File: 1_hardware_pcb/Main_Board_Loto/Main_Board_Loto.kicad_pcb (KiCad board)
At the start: 2 copper layers, 138 x 119 mm, 77 parts, among them J1 Conn_01x05_Pin, J1 FTDI, J2 Conn_01x05_Pin, J2 V+-, J3 Conn_01x05_Pin, J4 Conn_01x05_Pin, J5 MOTOR_PINM1A, J6 MOTOR_PINM1B, J7 MOTOR_PINM1A, J8 MOTOR_PINM1B, Q1 2N7002, SW1 SW_SPST, SW2 START, SW3 START, U1 AMS1117-3.3, U1 QRE1113GR, U2 LM7805_TO220, U2 QRE1113GR, U3 QRE1113GR, U3 TA6586, U4 ESP32-WROOM-32, U4 QRE1113GR, U5 QRE1113GR, U5 TA6586, U6 QRE1113GR, U7 QRE1113GR, U8 QRE1113GR

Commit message: SCH terminado
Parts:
- removed BOOT1, EN1: SW_Push, Button_Switch_THT:SW_PUSH_6mm_H5mm
- removed the C1 at (134.2, 80.1)
- removed the C1 at (147.7, 47.8)
- removed the C2 at (144.1, 46.8)
- removed the C2 at (98.4, 105.0)
- removed D3: LED, EESTN5-v2:Led_0805
- removed the H1 at (107.5, 46.5)
- removed the H1 at (112.1, 124.5)
- removed the H2 at (175.9, 124.5)
- removed the H2 at (180.5, 46.5)
- removed the J1 at (202.3, 110.1)
- removed the J1 at (162.3, 44.8)
- removed the J2 at (115.1, 44.8)
- removed the J2 at (97.0, 95.5)
- removed J6, J8: MOTOR_PINM1B, Connector:Banana_Jack_1Pin
- removed J7: MOTOR_PINM1A, Connector:Banana_Jack_1Pin
- removed the R1 at (194.2, 106.6)
- removed the R1 at (172.3, 35.1)
- removed the R2 at (183.2, 98.4)
- removed the R2 at (163.0, 35.1)
- removed the R3 at (113.2, 113.5)
- removed the R3 at (153.7, 35.1)
- removed the R4 at (116.9, 113.5)
- removed the R4 at (144.5, 35.1)
- removed the R5 at (178.9, 40.0)
- removed the R5 at (116.3, 107.9)
- removed the R6 at (120.5, 113.5)
- removed the R6 at (169.6, 40.0)
- removed the R7 at (160.3, 40.0)
- removed the R7 at (124.8, 107.9)
- removed the R8 at (171.6, 109.7)
- removed the R8 at (151.1, 40.0)
- removed the U1 at (140.5, 83.5)
- removed the U1 at (176.4, 36.9)
- removed the U2 at (101.8, 103.5)
- removed the U2 at (167.1, 36.9)
- removed the U3 at (138.6, 133.3)
- removed the U3 at (157.8, 36.9)
- removed the U4 at (140.2, 110.5)
- removed the U4 at (148.5, 36.9)
- removed the U5 at (156.9, 133.3)
- removed the U5 at (139.2, 36.9)
- added C1: 1uF, Capacitor_SMD:C_0805_2012Metric_Pad1.18x1.45mm_HandSolder, B.Cu at (400.8, 82.1)
- added C2: 1uF, Capacitor_SMD:C_0805_2012Metric_Pad1.18x1.45mm_HandSolder, B.Cu at (397.8, 87.3)
- added G***: LOGO, LOGO, F.Cu at (432.3, 115.2)
- added H1: Mounting_Hole, EESTN5:hole_3mm, F.Cu at (399.4, 111.4)
- added H2: Mounting_Hole, EESTN5:hole_3mm, F.Cu at (399.4, 134.8)
- added H7: HOLE, EESTN5:Separador_M3_5mm, F.Cu at (437.2, 168.2)
- added H8: HOLE, EESTN5:Separador_M3_5mm, F.Cu at (437.2, 175.4)
- added J1: V+-, EESTN5:BORNERA2_AZUL, F.Cu at (380.4, 101.8)
- added J2: MOTOR_PINM1A, Connector:Banana_Jack_1Pin, F.Cu at (425.4, 152.6)
- added R1: 220, EESTN5:R_1206, B.Cu at (406.9, 98.3)
- added R17: 100, EESTN5:R_1206, B.Cu at (391.9, 46.7)
- added R18: 10k, EESTN5:R_1206, B.Cu at (425.7, 45.9)
- added R19: 10k, EESTN5:R_1206, B.Cu at (413.9, 47.6)
- added R2: 4K7, EESTN5:R_1206, B.Cu at (462.4, 102.4)
- added R20: 10k, EESTN5:R_1206, B.Cu at (402.0, 48.7)
- added R21: 10k, EESTN5:R_1206, B.Cu at (391.9, 50.2)
- added R3: 220, EESTN5:R_1206, B.Cu at (407.0, 105.5)
- added R4: 10K, EESTN5:R_1206, B.Cu at (428.6, 96.0)
- added R5: 4K7, EESTN5:R_1206, B.Cu at (471.7, 102.8)
- added R6: 100, EESTN5:R_1206, B.Cu at (470.4, 53.4)
- added R7: 100, EESTN5:R_1206, B.Cu at (460.7, 49.8)
- added R8: 100, EESTN5:R_1206, B.Cu at (449.6, 44.4)
- added U1: AMS1117-3.3, Package_TO_SOT_SMD:SOT-223-3_TabPin2, B.Cu at (407.1, 78.5)
- added U10: QRE1113GR, OptoDevice:OnSemi_CASE100CY, B.Cu at (425.7, 39.1)
- added U11: QRE1113GR, OptoDevice:OnSemi_CASE100CY, B.Cu at (413.8, 40.5)
- added U12: QRE1113GR, OptoDevice:OnSemi_CASE100CY, B.Cu at (401.9, 41.9)
- added U13: QRE1113GR, OptoDevice:OnSemi_CASE100CY, B.Cu at (391.8, 43.5)
- added U2: LM7805_TO220, Package_TO_SOT_THT:TO-220-3_Vertical, F.Cu at (395.9, 91.1)
- added U3: TA6586, Package_DIP:DIP-8_W7.62mm, F.Cu at (423.5, 136.1)
- added U4: ESP32_DevKit_V1_CH9102X, EESTN5:ESP32_DevKit_V1_CH9102X, F.Cu at (433.3, 100.4)
- added U5: TA6586, Package_DIP:DIP-8_W7.62mm, F.Cu at (454.2, 136.2)
- added U9: QRE1113GR, OptoDevice:OnSemi_CASE100CY, B.Cu at (437.1, 39.2)
- BZ1: footprint EESTN5-v2:Buzzer_12mm -> EESTN5:Buzzer_12mm
- C3: value 1n -> 1uF; footprint EESTN5-v2:C_0805 -> Capacitor_SMD:C_0805_2012Metric_Pad1.18x1.45mm_HandSolder
- C5: value 1uF -> 0.1uF; footprint Capacitor_SMD:C_0805_2012Metric_Pad1.18x1.45mm_HandSolder -> EESTN5:C_0805
- C6: value 1n -> 100uF; footprint EESTN5-v2:C_0805 -> Capacitor_THT:CP_Radial_D5.0mm_P2.50mm; moved to F.Cu
- C7: value 0.1uF -> 100nf; footprint EESTN5-v2:C_0805 -> Capacitor_SMD:C_0805_2012Metric_Pad1.18x1.45mm_HandSolder
- C8: value 100uF -> 100uf; footprint Capacitor_THT:CP_Radial_D5.0mm_P2.50mm -> Capacitor_THT:C_Radial_D5.0mm_H11.0mm_P2.00mm
- C9: footprint EESTN5-v2:C_0805 -> EESTN5:C_0805
- D1, D2: footprint EESTN5-v2:Led_0805 -> EESTN5:led_5mm_clear
- H3, H4, H5, H6: footprint EESTN5-v2:hole_3mm -> EESTN5:hole_3mm
- J3: value Conn_01x05_Pin -> MOTOR_PINM1B; footprint Connector_PinHeader_2.54mm:PinHeader_1x05_P2.54mm_Horizontal -> Connector:Banana_Jack_1Pin
- J4: value Conn_01x05_Pin -> MOTOR_PINM1A; footprint Connector_PinHeader_2.54mm:PinHeader_1x05_P2.54mm_Horizontal -> Connector:Banana_Jack_1Pin
- J5: value MOTOR_PINM1A -> MOTOR_PINM1B
- R10, R11, R12: value 100 -> 10k; footprint EESTN5-v2:R_0805 -> EESTN5:R_1206
- R13, R9: footprint EESTN5-v2:R_0805 -> EESTN5:R_1206
- R14, R15, R16: value 10k -> 100; footprint EESTN5-v2:R_0805 -> EESTN5:R_1206
- SW1: value SW_SPST -> START; footprint EESTN5-v2:SW_SPDT_TH_Vertical -> Button_Switch_THT:SW_PUSH_6mm_H5mm
- SW2: value START -> SW_SPST; footprint Button_Switch_THT:SW_PUSH_6mm_H5mm -> EESTN5:SW_SPDT_TH_Vertical
- moved SW1 372.8 mm to (462.4, 93.9), turned to 0 degrees
- moved SW3 353.1 mm to (471.9, 93.9), turned to 0 degrees
- moved H4 351.6 mm to (463.4, 134.8), turned to 0 degrees
- moved J4 347.2 mm to (456.4, 152.8), turned to 0 degrees
- moved R10 344.8 mm to (470.4, 48.9), turned to 0 degrees
- moved R11 344.3 mm to (460.7, 45.0), turned to 0 degrees
- moved R12 342.6 mm to (449.6, 47.8), turned to 0 degrees
- moved U6 340.6 mm to (470.4, 45.7)
- moved U7 340.1 mm to (460.7, 42.1)
- moved U8 338.3 mm to (449.6, 40.9)
- moved C8 337.2 mm to (455.7, 75.2), turned to 180 degrees
- moved H6 334.6 mm to (429.9, 175.4), turned to 0 degrees
- moved C7 317.5 mm to (455.7, 82.2), turned to 180 degrees
- moved C9 316.2 mm to (444.4, 135.0)
- moved C5 310.6 mm to (413.7, 134.9), turned to -90 degrees
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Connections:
- C3 pad 1: GND -> +3V3
- C3 pad 2: /BOOT -> GND
- C4 pad 1: +3V3 -> +5V
- C5 pad 1: +5V -> VCC
- C6 pad 1: GND -> VCC
- C6 pad 2: /EN -> GND
- C7 pad 1: VCC -> +3V3
- C8 pad 1: VCC -> +3V3
- J3 pad 1: /OUT_4 -> /OUTM1B
- J4 pad 1: /OUT_8 -> /OUTM2A
- J5 pad 1: /OUTM1A -> /OUTM2B
- R10 pad 1: +3V3 -> /OUT_1
- R10 pad 2: Net-(U6-A) -> +3V3
- R11 pad 1: +3V3 -> /OUT_2
- R11 pad 2: Net-(U7-A) -> +3V3
- R12 pad 1: +3V3 -> /OUT_3
- R12 pad 2: Net-(U8-A) -> +3V3
- R13 pad 1: /OUT_5 -> /OUT_4
- R14 pad 1: /OUT_6 -> +3V3
- R14 pad 2: +3V3 -> Net-(U10-A)
- R15 pad 1: /OUT_7 -> +3V3
- R15 pad 2: +3V3 -> Net-(U11-A)
- R16 pad 1: /OUT_8 -> +3V3
- R16 pad 2: +3V3 -> Net-(U12-A)
- SW1 pad 1: VCC -> GND
- SW1 pad 2: Net-(SW1-B) -> /PUSH_1
- SW2 pad 1: GND -> VCC
- SW2 pad 2: /PUSH_1 -> Net-(SW2-B)
- U6 pad 3: /OUT_6 -> /OUT_1
- U7 pad 3: /OUT_7 -> /OUT_2
- U8 pad 3: /OUT_8 -> /OUT_3
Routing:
- net +3V3: track 369.3 -> 158.7 mm, vias 1 -> 0
- net /BOOT: track 102.2 -> 0.00 mm, vias 3 -> 0
- net +5V: track 137.7 -> 42.9 mm, vias 2 -> 0
- net /Tx: track 71.6 -> 0.00 mm, vias 1 -> 0
- net /Rx: track 67.4 -> 0.00 mm, vias 1 -> 0
- net /EN: track 59.4 -> 0.00 mm, vias 1 -> 0
- net /BUZZER: track 51.3 -> 109.5 mm, vias 1 -> 0
- net /PUSH_1: track 44.3 -> 85.1 mm, vias 1 -> 0
- net /OUT_8: track 39.2 -> 77.7 mm
- net /PUSH_2: track 39.8 -> 71.9 mm, vias 1 -> 0
- net VCC: track 122.1 -> 94.6 mm
- net /OUT_7: track 37.2 -> 64.1 mm
- net /OUT_1: track 50.5 -> 77.1 mm
- net /OUT_2: track 47.2 -> 67.1 mm
- net Net-(SW2-B): track 0.00 -> 20.0 mm
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- removed copper zone on B.Cu, net /OUTM1A
- removed copper zone on F.Cu, net /OUTM1A
- removed copper zone on B.Cu, net /OUTM1B
- removed copper zone on F.Cu, net /OUTM1B
- removed copper zone on B.Cu, net /OUTM2A
- removed copper zone on F.Cu, net /OUTM2A
- removed copper zone on B.Cu, net /OUTM2B
- removed copper zone on F.Cu, net /OUTM2B
- removed copper zone on B.Cu, net GND
- removed copper zone on F.Cu, net GND
- removed copper zone on B.Cu, net VCC
- removed copper zone on F.Cu, net VCC
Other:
- board outline removed

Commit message: Definida la ubicacion de los componentes y enrutadas las vias de los mismos
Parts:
- removed the C2 at (397.8, 87.3)
- removed H5, H6: Mounting_Hole, EESTN5:hole_3mm
- removed H7, H8: HOLE, EESTN5:Separador_M3_5mm
- added C6: 100nf, Capacitor_SMD:C_0805_2012Metric_Pad1.18x1.45mm_HandSolder, B.Cu at (142.0, 47.2)
- moved C2 395.7 mm to (60.2, 86.7), turned to 90 degrees
- moved C5 391.8 mm to (65.7, 44.5), turned to 90 degrees
- moved R4 345.8 mm to (82.8, 96.5), turned to 0 degrees
- moved R7 337.2 mm to (123.8, 36.9), turned to 90 degrees
- moved R6 337.0 mm to (133.8, 38.2), turned to 90 degrees
- moved R8 336.0 mm to (113.8, 35.0), turned to 90 degrees
- moved Q1 335.6 mm to (87.9, 95.6), turned to 0 degrees
- moved R9 333.5 mm to (103.8, 33.8), turned to 90 degrees
- moved U7 332.4 mm to (128.2, 39.2)
- moved U6 332.2 mm to (138.2, 40.5)
- moved R14 332.1 mm to (93.8, 33.8), turned to 90 degrees
- moved U8 331.3 mm to (118.2, 37.3)
- moved SW1 331.3 mm to (131.1, 87.6)
- moved SW3 331.3 mm to (140.6, 87.6)
- moved R15 330.2 mm to (83.8, 35.3), turned to 90 degrees
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- renumbered C8 to C2, C7 to C5, C5 to C7, C6 to C8
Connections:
- C2 pad 1: +3V3 -> VCC
- J1 pad 2: VCC -> /SWITCH
- SW2 pad 1: VCC -> /SWITCH
- SW2 pad 2: Net-(SW2-B) -> VCC
- U2 pad 1: Net-(SW2-B) -> VCC
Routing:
- net GND: track 348.9 -> 122.4 mm, vias 0 -> 9
- net +3V3: track 158.7 -> 287.3 mm
- net /BUZZER: track 109.5 -> 45.5 mm
- net /LED_1: track 39.1 -> 86.9 mm
- net /LED_2: track 41.6 -> 76.7 mm
- net VCC: track 94.6 -> 121.3 mm
- net Net-(SW2-B): track 20.0 -> 0.00 mm
- net /SWITCH: track 0.00 -> 12.0 mm
- net /OUT_8: track 77.7 -> 68.2 mm
- net Net-(D1-A): track 11.6 -> 3.28 mm
- net Net-(D2-A): track 13.0 -> 5.65 mm
- net /OUT_7: track 64.1 -> 57.6 mm
- net /PUSH_2: track 71.9 -> 65.6 mm
- net Net-(BZ1-+): track 4.23 -> 10.4 mm
- net /PUSH_1: track 85.1 -> 79.8 mm
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- added copper zone on B.Cu, net GND
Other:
- board outline added: 138.7 x 158.6 mm

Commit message: Cntorno de PCB diseñad en FreeCAD y PCB terminad en Kicad
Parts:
- C2: footprint Capacitor_THT:C_Radial_D5.0mm_H11.0mm_P2.00mm -> Capacitor_THT:C_Radial_D10.0mm_H12.5mm_P5.00mm
- moved G*** 185.7 mm to (-82.5, 99.2)
- moved C2 118.1 mm to (177.9, 77.0), turned to 180 degrees
- moved C4 113.6 mm to (186.5, 63.9), turned to 180 degrees
- moved U2 113.1 mm to (182.5, 66.7), turned to 0 degrees
- moved U1 109.6 mm to (194.4, 66.2)
- moved C3 108.8 mm to (199.0, 61.5), turned to 180 degrees
- moved C1 108.5 mm to (186.5, 69.2)
- moved R2 106.0 mm to (239.9, 82.6), turned to 90 degrees
- moved R5 105.8 mm to (249.3, 82.6), turned to 90 degrees
- moved J3 105.8 mm to (190.4, 141.3)
- moved SW1 105.7 mm to (236.5, 79.0)
- moved SW3 105.7 mm to (246.0, 79.0)
- moved R4 105.2 mm to (187.6, 87.3)
- moved Q1 105.2 mm to (192.7, 86.3)
- moved BZ1 104.9 mm to (197.3, 82.5), turned to 90 degrees
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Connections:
- net /OUT_1 renamed /QRE_1
- net /OUT_2 renamed /QRE_2
- net /OUT_3 renamed /QRE_3
- net /OUT_4 renamed /QRE_4
- net /OUT_5 renamed /QRE_5
- net /OUT_6 renamed /QRE_6
- net /OUT_7 renamed /QRE_7
- net /OUT_8 renamed /QRE_8
- U4 pad 21: /PUSH_2 -> /PUSH_1
- U4 pad 22: /PUSH_1 -> /PUSH_2
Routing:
- net VCC: track 121.3 -> 77.2 mm
- net /PUSH_1: track 79.8 -> 48.9 mm
- net GND: track 122.4 -> 100.2 mm
- net /OUTM1A: track 19.0 -> 0.00 mm
- net /OUTM1B: track 17.1 -> 0.00 mm
- net /OUTM2A: track 15.2 -> 0.00 mm
- net /OUTM2B: track 14.6 -> 0.00 mm
- net +5V: track 40.2 -> 26.9 mm
- net /SWITCH: track 12.0 -> 0.00 mm
- net /PUSH_2: track 65.6 -> 56.6 mm
- net Net-(BZ1-+): track 10.4 -> 3.63 mm
- net /QRE_7: track 57.6 -> 54.4 mm
- net /M1A: track 34.3 -> 37.4 mm
- net /M1B: track 33.9 -> 37.0 mm
- net /QRE_6: track 51.2 -> 48.1 mm
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- added copper zone on B.Cu, net +3V3
- added copper zone on B.Cu, net /OUTM1A
- added copper zone on B.Cu, net /OUTM1B
- added copper zone on B.Cu, net /OUTM2A
- added copper zone on B.Cu, net /OUTM2B
- added copper zone on B.Cu, net /SWITCH
- added copper zone on B.Cu, net VCC
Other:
- board size 138.7 x 158.6 mm -> 138.1 x 157.3 mm

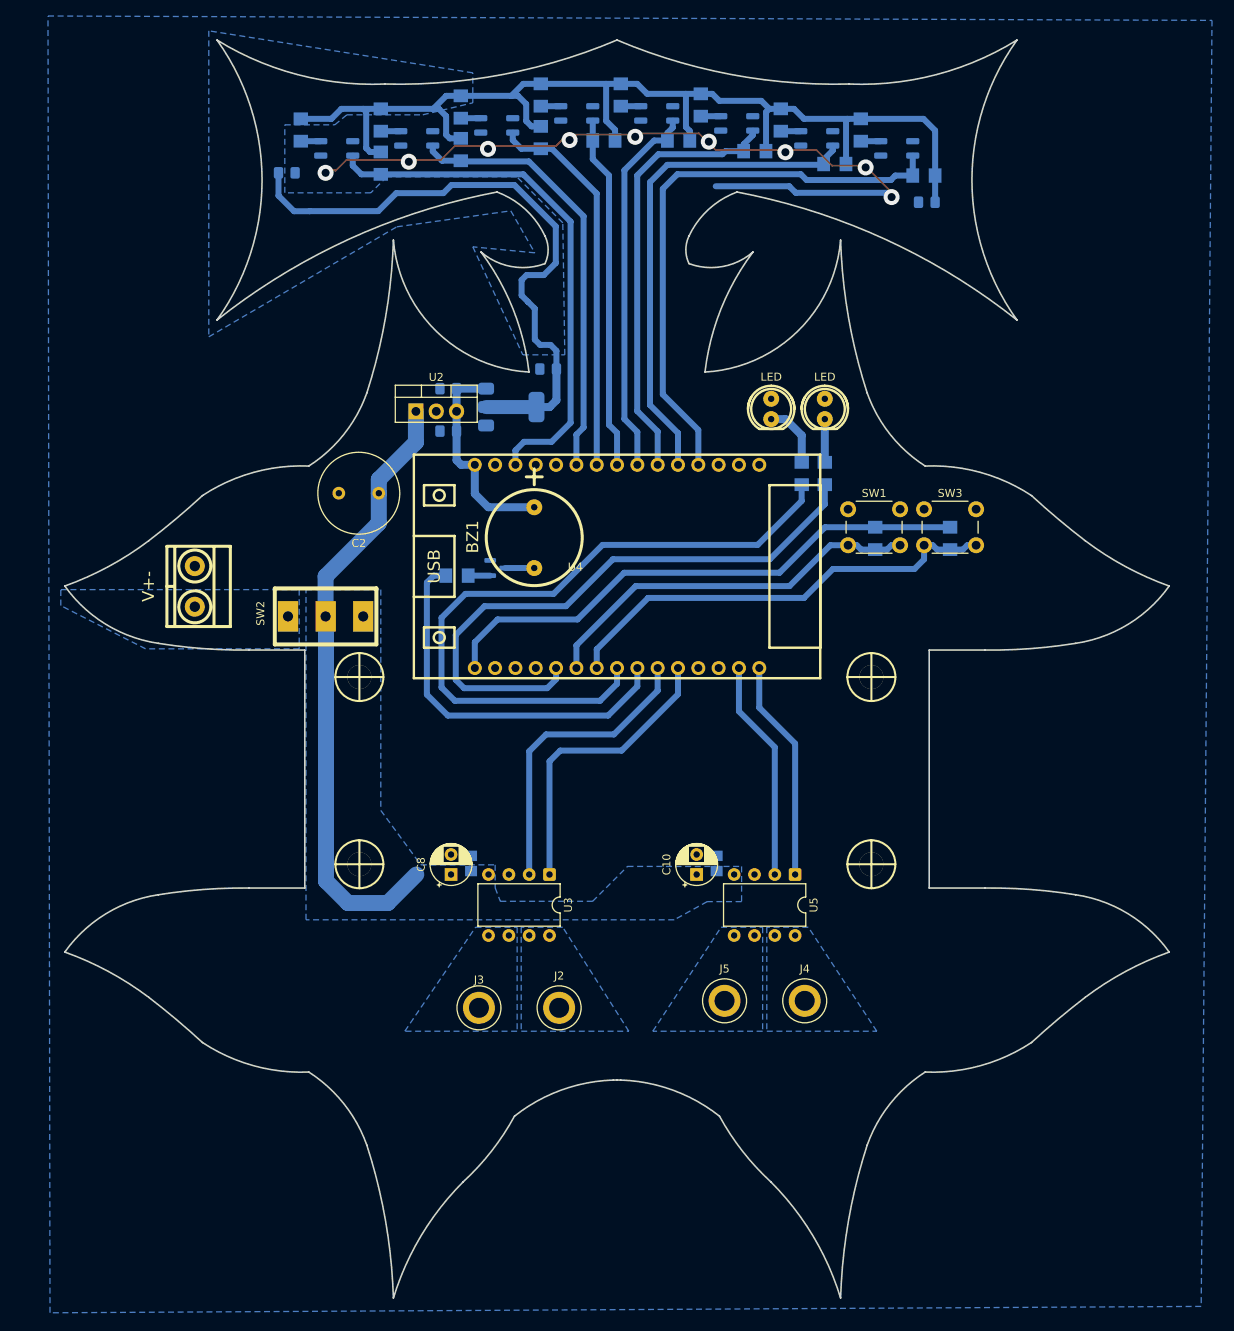
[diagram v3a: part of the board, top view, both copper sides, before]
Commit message: Soporte para motor incluido en el PCB y generadas las imagenes de fabricacion
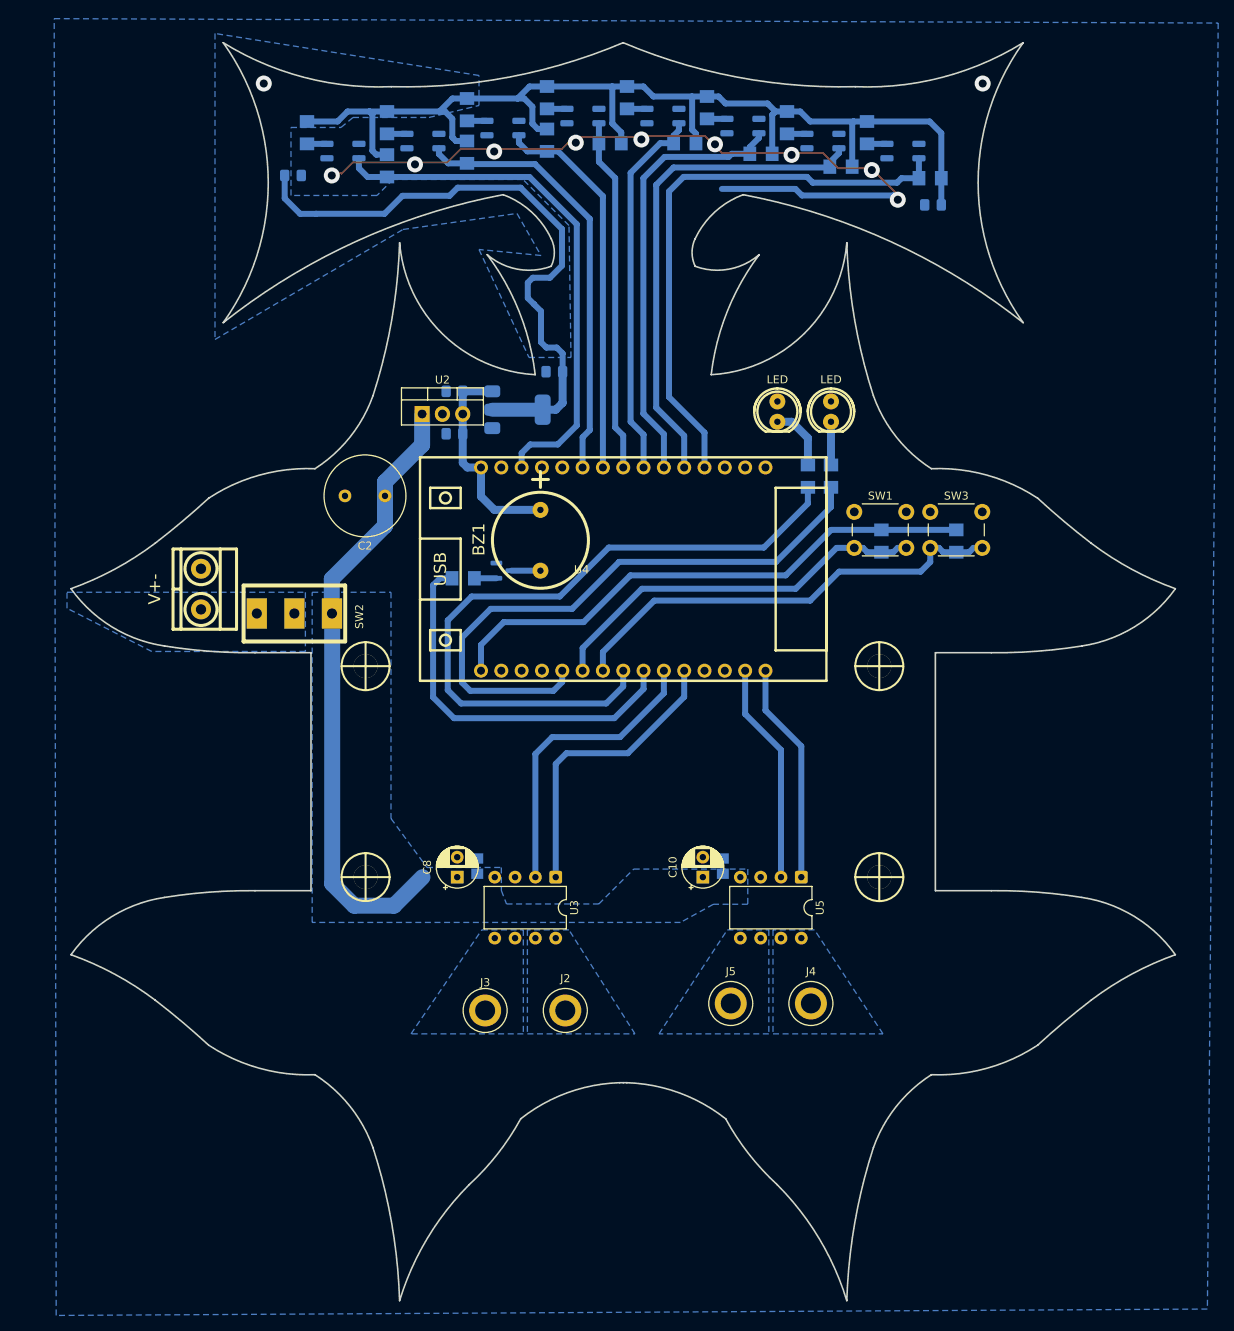
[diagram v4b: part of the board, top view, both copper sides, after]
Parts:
- moved SW2 3.92 mm to (167.3, 92.0), turned to -90 degrees
- moved H4 1.89 mm to (240.4, 125.0)
- moved H2 1.79 mm to (176.2, 125.0)
- moved H3 1.68 mm to (240.4, 98.6)
- moved H1 1.57 mm to (176.2, 98.6)
- moved D2 0.84 mm to (227.7, 66.8)
- moved R10 0.84 mm to (246.8, 37.6)
- moved R13 0.84 mm to (216.1, 33.2)
- moved BZ1 0.84 mm to (198.1, 82.9)
- moved C1 0.84 mm to (187.3, 69.5)
- moved C10 0.84 mm to (218.4, 125.0)
- moved C2 0.84 mm to (178.6, 77.3)
- moved C7 0.84 mm to (190.2, 123.6)
- moved C8 0.84 mm to (187.7, 125.0)
- moved C9 0.84 mm to (220.9, 123.6)
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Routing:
- net +3V3: vias 0 -> 1
- net GND: vias 9 -> 10

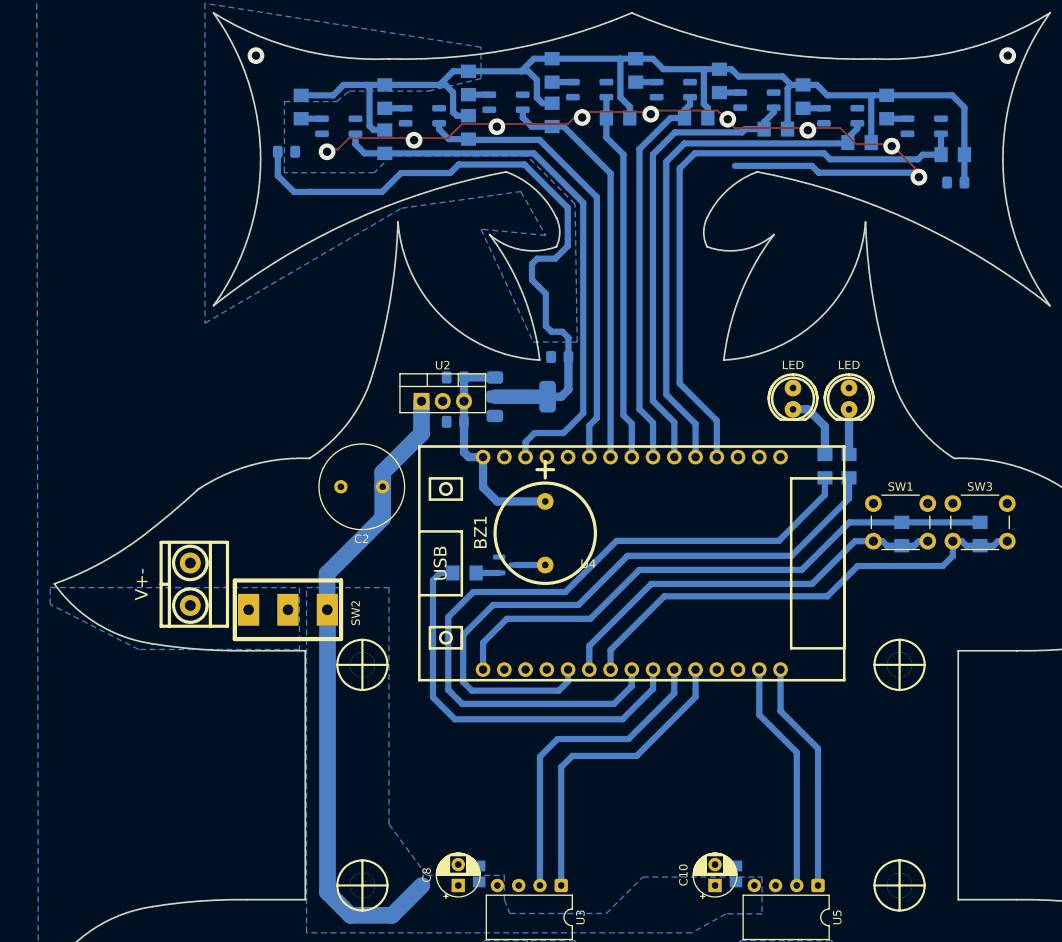
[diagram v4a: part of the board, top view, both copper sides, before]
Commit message: Pistas de 0.75 pasaron a 0.8 por temas de CNC
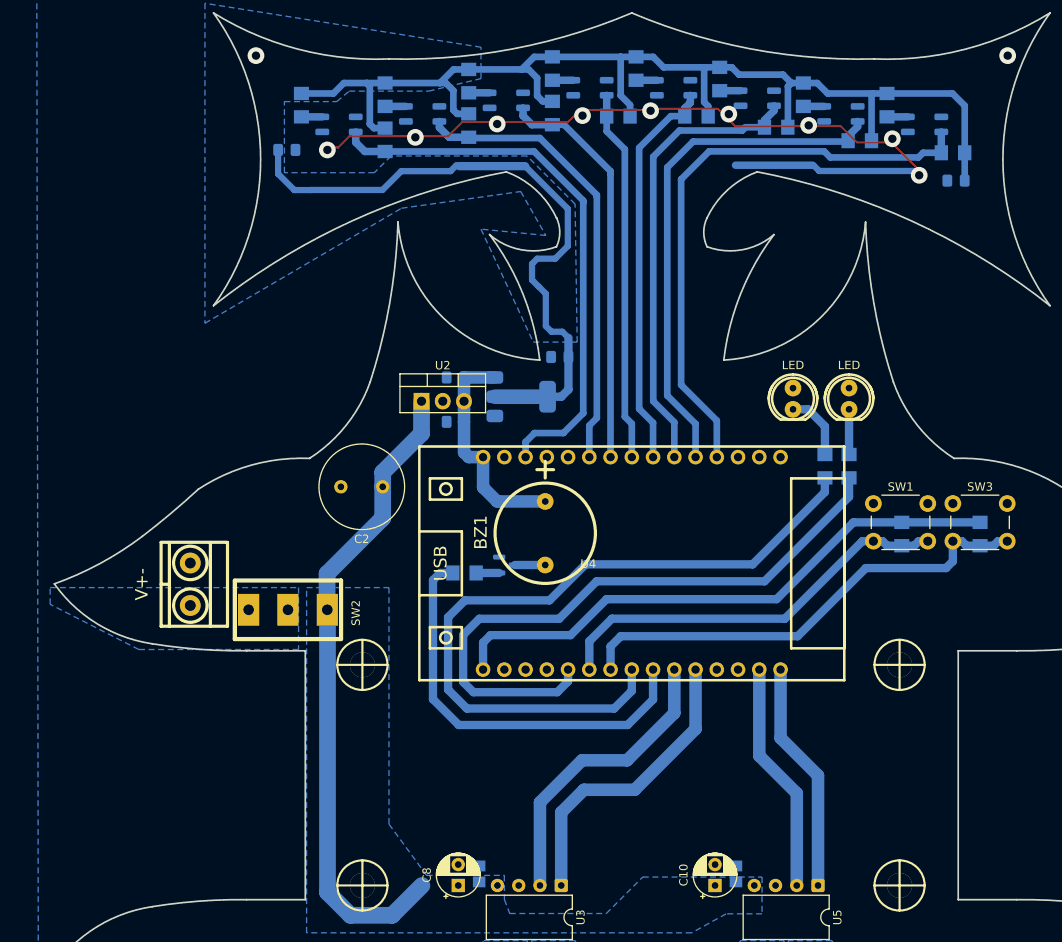
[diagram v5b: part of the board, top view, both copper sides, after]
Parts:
- moved C5 0.23 mm to (167.2, 37.0)
- moved R21 0.23 mm to (178.9, 35.8)
- moved R14 0.23 mm to (198.9, 27.3)
- moved R15 0.23 mm to (188.9, 28.8)
- moved R16 0.23 mm to (178.9, 30.4)
- moved R17 0.23 mm to (168.9, 31.7)
- moved R6 0.23 mm to (238.9, 31.7)
- moved R7 0.23 mm to (228.9, 30.4)
- moved R8 0.23 mm to (218.9, 28.6)
- moved R9 0.23 mm to (208.9, 27.3)
- moved U10 0.23 mm to (203.4, 29.6)
- moved U11 0.23 mm to (193.4, 31.1)
- moved U8 0.23 mm to (223.4, 30.9)
- moved U9 0.23 mm to (213.4, 29.6)
- moved R11 0.23 mm to (235.7, 35.9)
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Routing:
- net /M1A: track 37.4 -> 35.6 mm
- net /BUZZER: track 47.9 -> 49.4 mm
- net /M1B: track 37.0 -> 36.0 mm
- net /QRE_1: track 71.4 -> 70.5 mm
- net GND: track 100.2 -> 100.9 mm
- net /LED_1: track 87.3 -> 87.9 mm
- net /PUSH_2: track 56.6 -> 57.3 mm
